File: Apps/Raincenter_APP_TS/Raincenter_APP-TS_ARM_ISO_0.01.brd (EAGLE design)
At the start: 42.3 x 27.4 mm, 26 parts

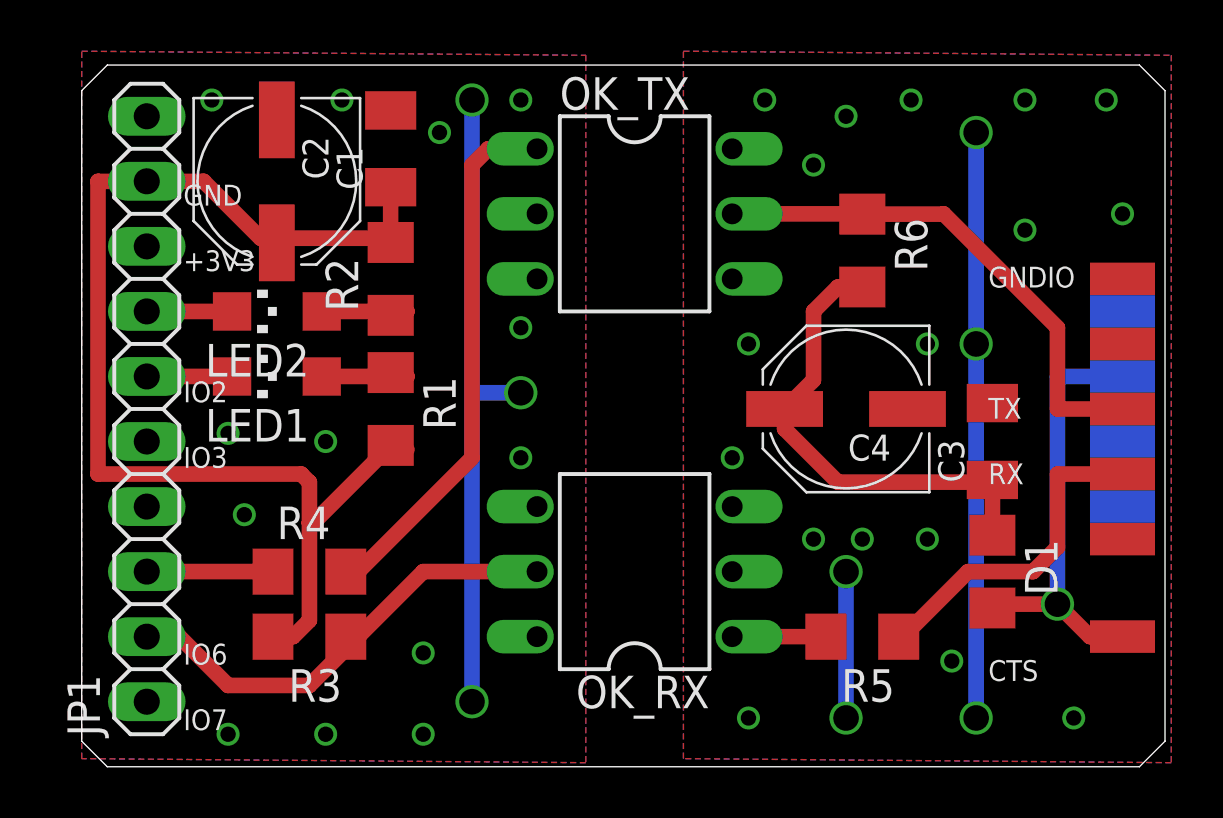
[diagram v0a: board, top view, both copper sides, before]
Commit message: Raincenter_APP: restored Ver. 0.01, changed wire width from 16mil to 24mil
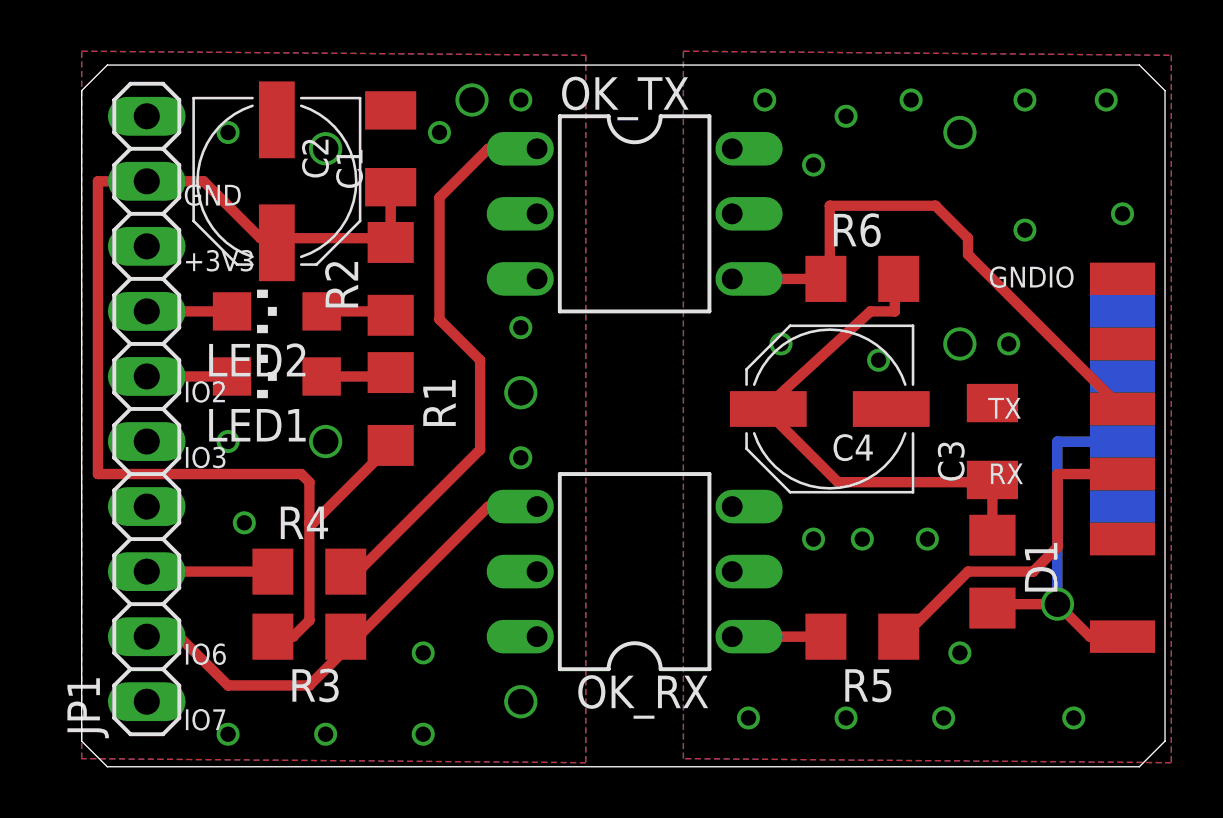
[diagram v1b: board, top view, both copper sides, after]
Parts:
- PAD10: value CTS -> RTS
- PAD7: value (none) -> RTS
- PAD8: value CTS -> (none)
- moved R6 1.11 mm to (30.5, 19.1), turned to 0 degrees
- moved C4 0.63 mm to (29.2, 14.0)
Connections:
- net GND: now also OK_RX.5; no longer OK_RX.4
- net GNDIO: now also OK_TX.5; no longer OK_TX.4
- net IO7: now also OK_RX.4; no longer OK_RX.5
- net RC_RTS: now also PAD7.1; no longer PAD8.1
- net RX_TX: now also OK_TX.4; no longer OK_TX.5
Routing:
- net GNDIO: track 28.6 -> 0.00 mm, vias 22 -> 21
- net GND: track 25.4 -> 0.00 mm
- net RC_RTS: track 17.2 -> 14.6 mm
- net RX_TX: track 20.3 -> 21.8 mm
- net N$10: track 21.0 -> 22.3 mm
- net IO7: track 18.7 -> 19.7 mm
- net V+: track 19.6 -> 20.1 mm
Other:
- board text added: "GNDIO TX RX"
- board text removed: "GNDIO TX RX CTS"
